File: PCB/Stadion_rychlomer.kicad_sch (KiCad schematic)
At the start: 65 parts, among them J1 USB_B_Micro, J2 OLED I2C, J3 ICSP, J4 Conn_01x03_Pin, J5 SPÍD & PWR, J6 AUX DDAA, J7 ENG RPM, Q1 140817143200, Q2 PC817, U1 Mikroprofesor, U2 FT232RL, U3 LM1117MP-5.0, Y1 16MHz

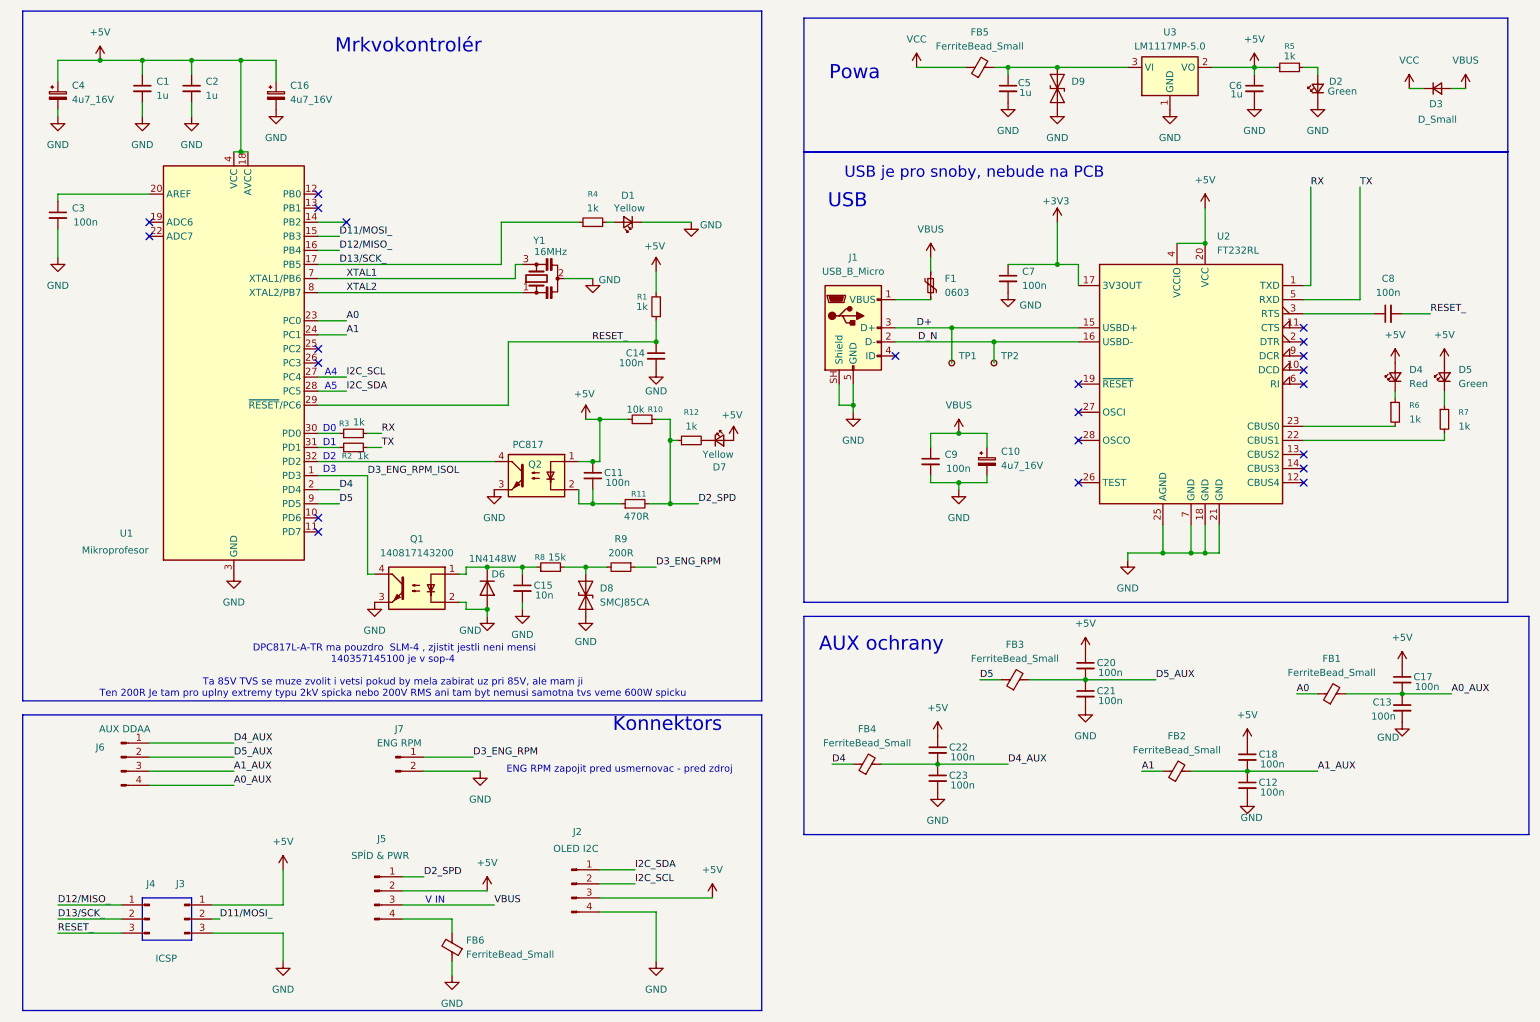
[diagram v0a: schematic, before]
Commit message: Updated PNs, minor tweaks on PCB
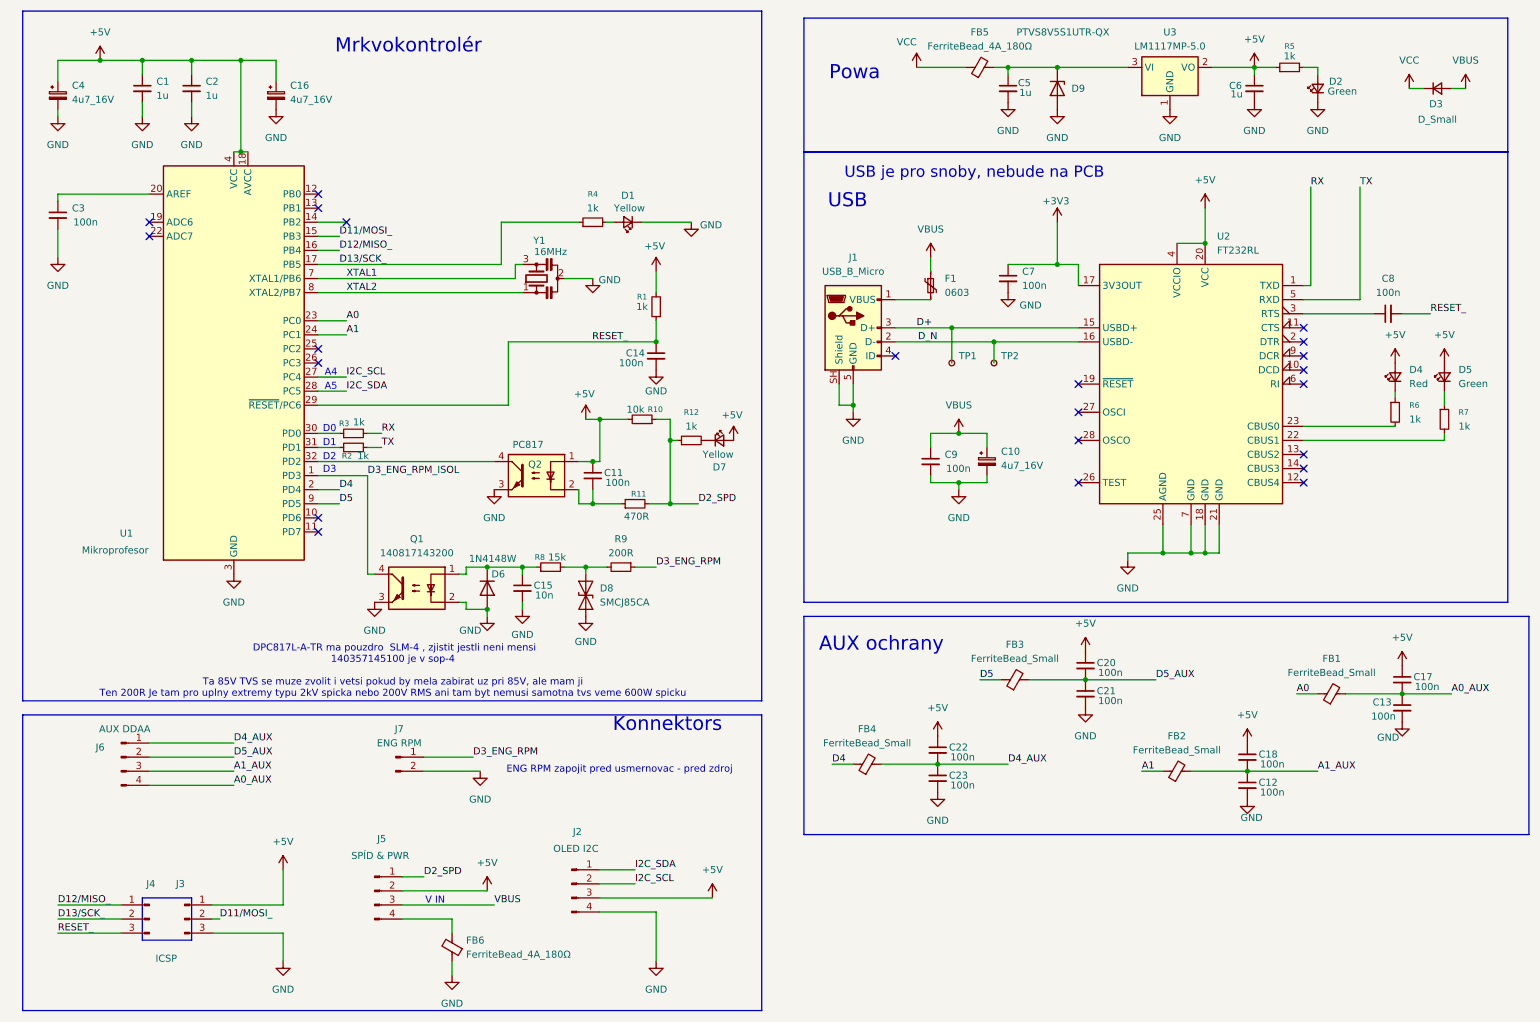
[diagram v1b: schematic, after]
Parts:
- D9: value SMCJ85CA -> PTVS8V5S1UTR-QX; footprint Diode_SMD:D_SOD-123F -> AERO_Diode_SMD:D_SOD-123FL; symbol AERO_Power_Protection:SMCJ85CA -> Diode:PESD3V3U1UL; PN SMCJ85CA -> PTVS8V5S1UTR-QX; Supplier PN 576-SMCJ85CA -> 771-PTVS8V5S1UTR-QX
- FB5, FB6: value FerriteBead_Small -> FerriteBead_4A_180Ω; symbol Device:FerriteBead_Small -> AERO_FerriteBead:FerriteBead_4A_180Ohm_0806; PN (none) -> NFZ2MSD181SZ10L; Supplier (none) -> Mouser Electronics; Supplier Link (none) -> https://cz.mouser.com/ProductDetail/Murata-Electronics/NFZ2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; Supplier PN (none) -> 81-NFZ2MSD181SZ10L
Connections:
- net GND: now also D9.2 (A); no longer D9.1 (A1)
- net at C5.1, FB5.2, U3.3 (VI): now also D9.1 (K); no longer D9.2 (A2)
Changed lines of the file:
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@@
 	)
 	(junction
-		(at 199.39 26.67)
-		(diameter 0)
-		(color 0 0 0 0)
-	)
-	(junction
 		(at 226.06 114.3)
 		(diameter 0)
@@
 	)
 	(junction
+		(at 199.39 26.67)
+		(diameter 0)
+		(color 0 0 0 0)
+	)
+	(junction
 		(at 52.07 41.91)
 		(diameter 0)
@@
 	(wire
 		(pts
+			(xy 199.39 26.67) (xy 212.09 26.67)
+		)
+		(stroke
+			(width 0)
+			(type default)
+		)
+	)
+	(wire
+		(pts
 			(xy 58.42 29.21) (xy 58.42 25.4)
 		)
@@
 	(wire
 		(pts
-			(xy 199.39 26.67) (xy 212.09 26.67)
-		)
-		(stroke
-			(width 0)
-			(type default)
-		)
-	)
-	(wire
-		(pts
 			(xy 34.29 25.4) (xy 34.29 27.94)
 		)
@@
 		(in_pos_files yes)
 		(dnp no)
-		(fields_autoplaced yes)
 		(property "Reference" "#PWR011"
 			(at 173.99 30.48 0)
@@
 		)
 		(property "Value" "VCC"
-			(at 173.99 21.59 0)
+			(at 172.212 22.098 0)
 			(show_name no)
 			(do_not_autoplace no)
@@
 	)
 	(symbol
-		(lib_id "Device:FerriteBead_Small")
+		(lib_id "AERO_FerriteBead:FerriteBead_4A_180Ohm_0806")
 		(at 185.42 26.67 90)
 		(unit 1)
@@
 			)
 		)
-		(property "Value" "FerriteBead_Small"
+		(property "Value" "FerriteBead_4A_180Ω"
 			(at 185.3819 22.86 90)
 			(show_name no)
@@
 			)
 		)
-		(property "Datasheet" ""
+		(property "Datasheet" "https://cz.mouser.com/datasheet/2/281/murata_mure-s-a0008530226-1-1763711.pdf"
 			(at 185.42 26.67 0)
 			(hide yes)
@@
 			)
 		)
-		(property "Description" "Ferrite bead, small symbol"
+		(property "Description" "Ferrite Beads EMI Filter SMD 180ohm INFOTMT  4A  22mOhm DC resistance"
+			(at 185.42 26.67 0)
+			(hide yes)
+			(show_name no)
+			(do_not_autoplace no)
+			(effects
+				(font
+					(size 1.27 1.27)
+				)
+			)
+		)
+		(property "Supplier" "Mouser Electronics"
+			(at 185.42 26.67 0)
+			(hide yes)
+			(show_name no)
+			(do_not_autoplace no)
+			(effects
+				(font
+					(size 1.27 1.27)
+				)
+			)
+		)
+		(property "PN" "NFZ2MSD181SZ10L"
+			(at 185.42 26.67 0)
+			(hide yes)
+			(show_name no)
+			(do_not_autoplace no)
+			(effects
+				(font
+					(size 1.27 1.27)
+				)
+			)
+		)
+		(property "Supplier PN" "81-NFZ2MSD181SZ10L"
+			(at 185.42 26.67 0)
+			(hide yes)
+			(show_name no)
+			(do_not_autoplace no)
+			(effects
+				(font
+					(size 1.27 1.27)
+				)
+			)
+		)
+		(property "Supplier Link" "https://cz.mouser.com/ProductDetail/Murata-Electronics/NFZ2MSD181SZ10L?qs=rkhjVJ6%2F3EI5R7nKRbJ7XA%3D%3D"
 			(at 185.42 26.67 0)
 			(hide yes)
@@
 	)
 	(symbol
-		(lib_id "Device:FerriteBead_Small")
+		(lib_id "AERO_FerriteBead:FerriteBead_4A_180Ohm_0806")
 		(at 90.17 185.42 180)
 		(unit 1)
@@
 			)
 		)
-		(property "Value" "FerriteBead_Small"
+		(property "Value" "FerriteBead_4A_180Ω"
 			(at 92.71 186.728 0)
 			(show_name no)
@@
 			)
 		)
-		(property "Datasheet" ""
+		(property "Datasheet" "https://cz.mouser.com/datasheet/2/281/murata_mure-s-a0008530226-1-1763711.pdf"
 			(at 90.17 185.42 0)
 			(hide yes)
@@
 			)
 		)
-		(property "Description" "Ferrite bead, small symbol"
+		(property "Description" "Ferrite Beads EMI Filter SMD 180ohm INFOTMT  4A  22mOhm DC resistance"
+			(at 90.17 185.42 0)
+			(hide yes)
+			(show_name no)
+			(do_not_autoplace no)
+			(effects
+				(font
+					(size 1.27 1.27)
+				)
+			)
+		)
+		(property "Supplier" "Mouser Electronics"
+			(at 90.17 185.42 0)
+			(hide yes)
+			(show_name no)
+			(do_not_autoplace no)
+			(effects
+				(font
+					(size 1.27 1.27)
+				)
+			)
+		)
+		(property "PN" "NFZ2MSD181SZ10L"
+			(at 90.17 185.42 0)
+			(hide yes)
+			(show_name no)
+			(do_not_autoplace no)
+			(effects
+				(font
+					(size 1.27 1.27)
+				)
+			)
+		)
+		(property "Supplier PN" "81-NFZ2MSD181SZ10L"
+			(at 90.17 185.42 0)
+			(hide yes)
+			(show_name no)
+			(do_not_autoplace no)
+			(effects
+				(font
+					(size 1.27 1.27)
+				)
+			)
+		)
+		(property "Supplier Link" "https://cz.mouser.com/ProductDetail/Murata-Electronics/NFZ2MSD181SZ10L?qs=rkhjVJ6%2F3EI5R7nKRbJ7XA%3D%3D"
 			(at 90.17 185.42 0)
 			(hide yes)
@@
 	)
 	(symbol
-		(lib_id "AERO_Power_Protection:SMCJ85CA")
-		(at 199.39 30.48 90)
+		(lib_id "Diode:PESD3V3U1UL")
+		(at 199.39 30.48 270)
 		(unit 1)
 		(body_style 1)
@@
 		(in_pos_files yes)
 		(dnp no)
-		(fields_autoplaced yes)
 		(property "Reference" "D9"
-			(at 201.93 29.2099 90)
+			(at 201.93 30.4799 90)
 			(show_name no)
 			(do_not_autoplace no)
@@
 					(size 1.27 1.27)
 				)
-				(justify right)
+				(justify left)
 			)
 		)
-		(property "Value" "SMCJ85CA"
-			(at 201.93 31.7499 90)
-			(hide yes)
+		(property "Value" "PTVS8V5S1UTR-QX"
+			(at 208.788 20.32 90)
 			(show_name no)
 			(do_not_autoplace no)
@@
 			)
 		)
-		(property "Footprint" "Diode_SMD:D_SOD-123F"
-			(at 204.47 30.48 0)
+		(property "Footprint" "AERO_Diode_SMD:D_SOD-123FL"
+			(at 194.31 30.48 0)
 			(hide yes)
 			(show_name no)
@@
 			)
 		)
-		(property "Datasheet" "https://cz.mouser.com/datasheet/2/240/media-3320072.pdf"
-			(at 199.39 30.48 0)
+		(property "Datasheet" "https://assets.nexperia.com/documents/data-sheet/PTVSXS1UTR-Q_SER.pdf"
+			(at 204.47 30.48 0)
 			(hide yes)
 			(show_name no)
@@
 			)
 		)
-		(property "Description" "ESD Suppressors / TVS Diodes 1.5kW 85V 5% Bi-Directional Ipp:11A Vclamp: 137V Vbrkdn: 94.4V"
-			(at 199.39 30.48 0)
+		(property "Description" "Ochranné diody proti elektrostatickým výbojům/diody pro potlačení napětí z přechodových jevů PTVS8V5S1UTR-Q/SOD123W/CFP3"
+			(at 207.01 30.48 0)
 			(hide yes)
 			(show_name no)
@@
 			)
 		)
-		(property "PN" "SMCJ85CA"
+		(property "PN" " PTVS8V5S1UTR-QX "
 			(at 199.39 30.48 0)
 			(hide yes)
@@
 			)
 		)
-		(property "Supplier PN" "576-SMCJ85CA"
+		(property "Supplier PN" " 771-PTVS8V5S1UTR-QX "
 			(at 199.39 30.48 0)
 			(hide yes)
